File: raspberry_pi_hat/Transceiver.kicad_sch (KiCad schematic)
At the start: 6 parts, among them IC2 LM3940IT, J2 USB_C_Receptacle_PowerOnly_6P, J3 GPIO, U1 NRF24L01P

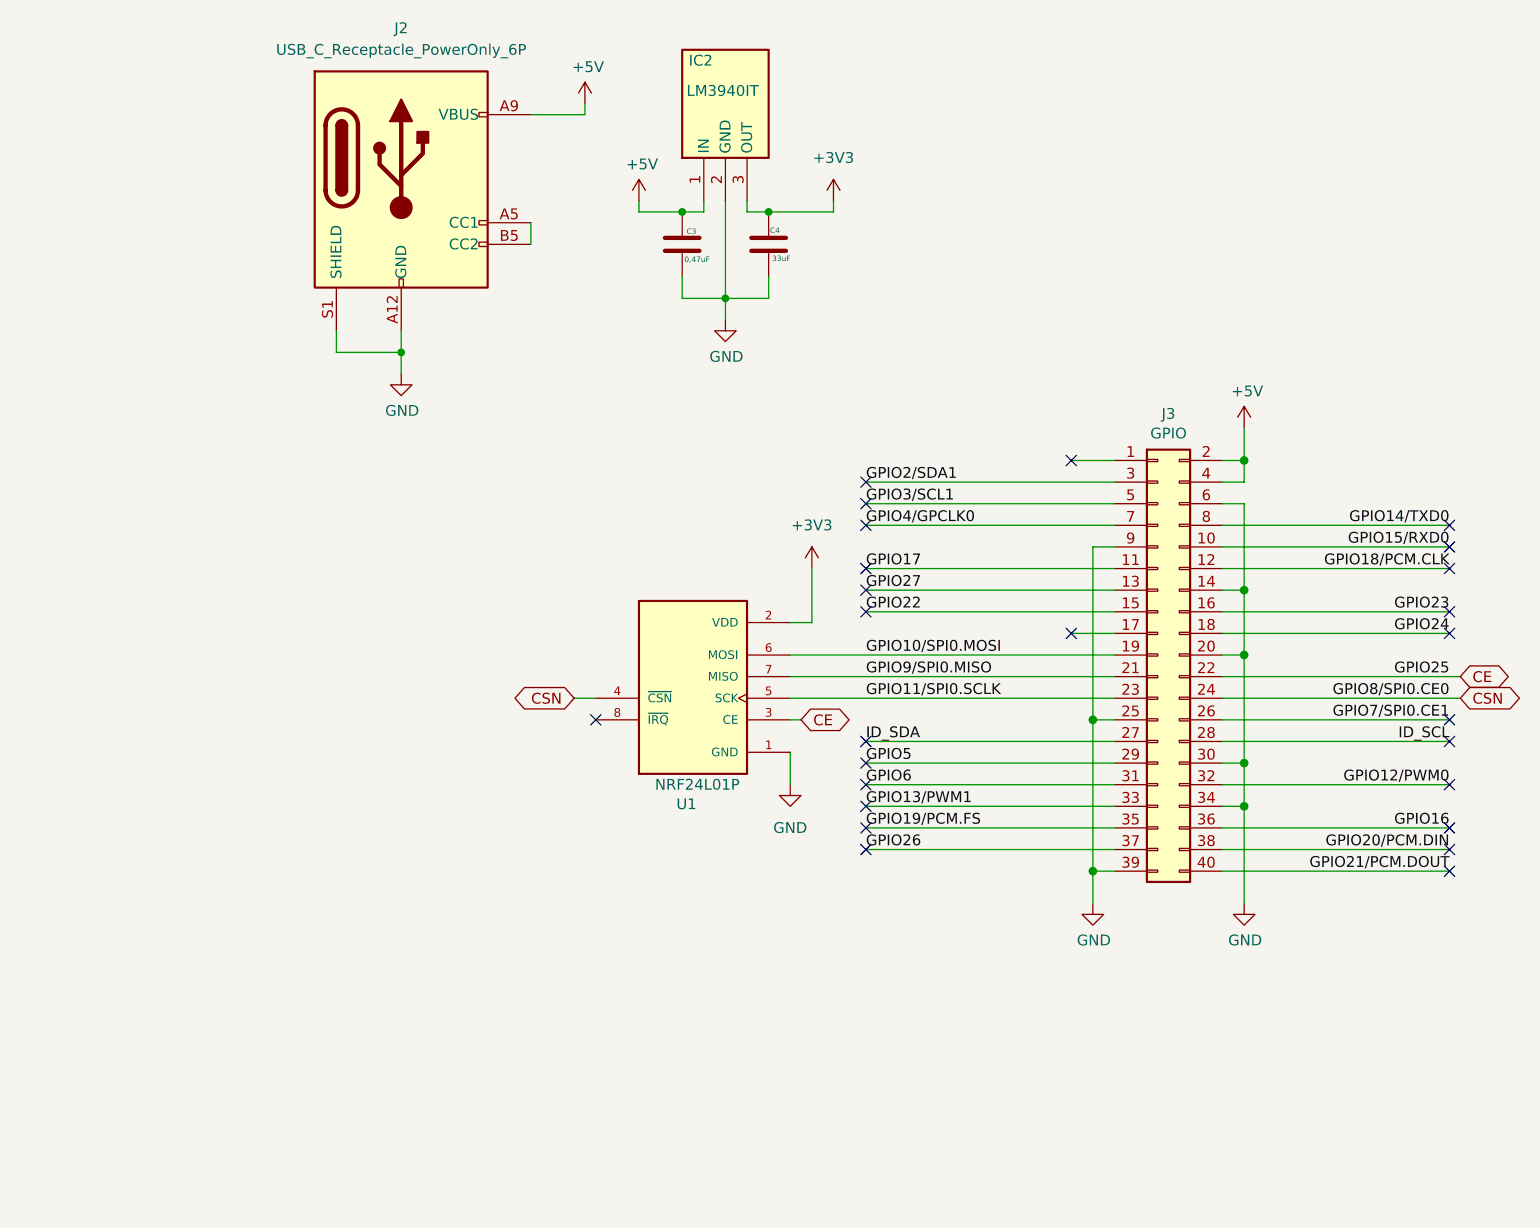
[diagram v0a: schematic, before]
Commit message: Solved split connection issues between boards
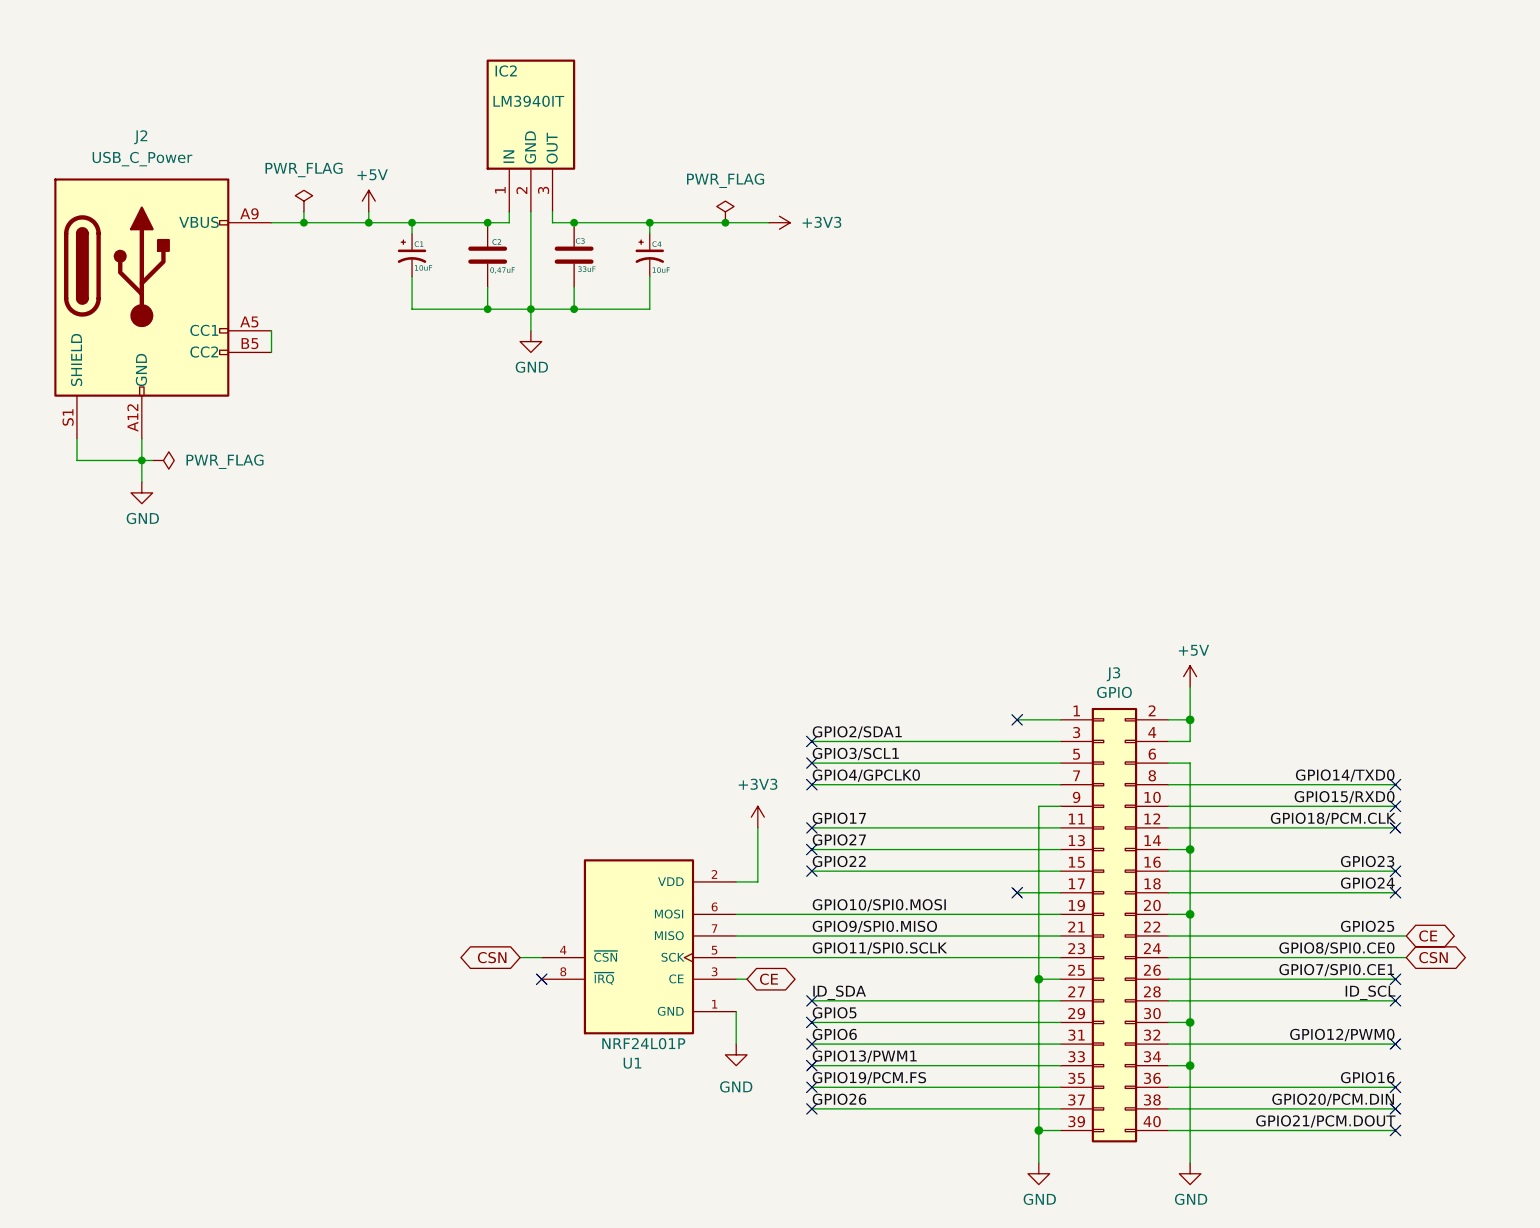
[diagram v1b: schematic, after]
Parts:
- added C1, C4: 10uF, Capacitor_THT:CP_Radial_D5.0mm_P2.50mm, symbol Device:C_Polarized_Small_US
- IC2: footprint Package_TO_SOT_THT:TO-262-3-1EP_Horizontal_TabDown -> Package_TO_SOT_THT:TO-220F-3_Horizontal_TabDown
- J2: value USB_C_Receptacle_PowerOnly_6P -> USB_C_Power
- renumbered C3 to C2, C4 to C3
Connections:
- net +3V3: now also C4.1
- net +5V: now also C1.1
- net GND: now also C1.2, C4.2
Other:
- moved on the sheet: C2, C3, IC2, J2, J3, U1

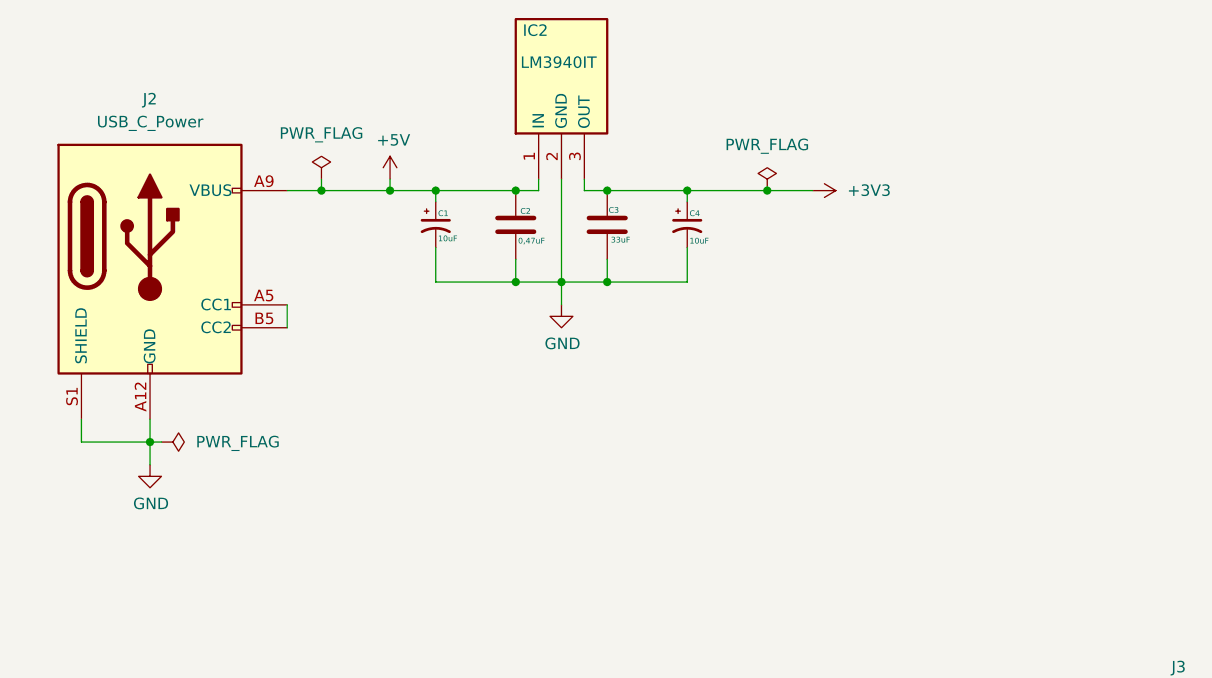
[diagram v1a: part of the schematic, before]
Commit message: Changed boards orientation and redistribution of components, still being 2 boards
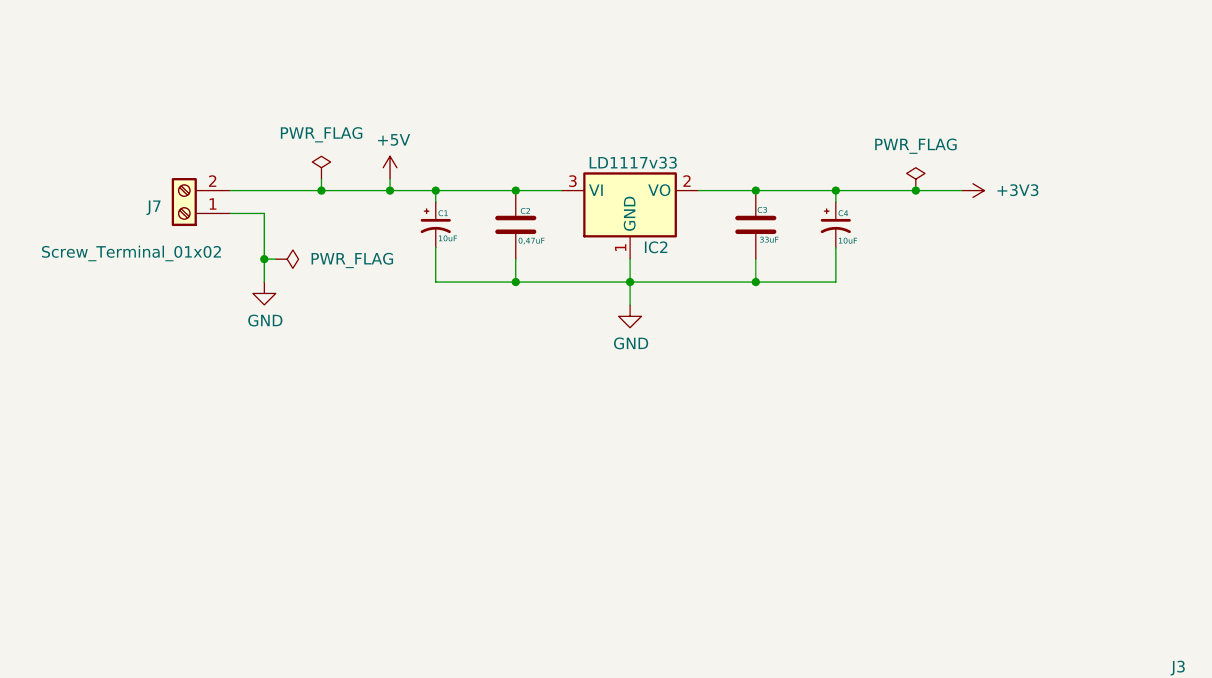
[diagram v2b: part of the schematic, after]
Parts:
- removed J2: USB_C_Power, Connector_USB:USB_C_Receptacle_GCT_USB4125-xx-x-0190_6P_TopMnt_Horizontal, symbol Connector:USB_C_Receptacle_PowerOnly_6P
- added J7: Screw_Terminal_01x02, TerminalBlock_MetzConnect:TerminalBlock_MetzConnect_Type101_RT01602HBWC_1x02_P5.08mm_Horizontal, symbol Connector:Screw_Terminal_01x02
- IC2: value LM3940IT -> LD1117v33; footprint Package_TO_SOT_THT:TO-220F-3_Horizontal_TabDown -> Package_TO_SOT_THT:TO-220-3_Vertical; symbol LM3940IT-3_3-NOPB:LM3940IT-3.3_NOPB -> Regulator_Linear:LD1117S33TR_SOT223
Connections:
- net +3V3: now also IC2.2 (VO); no longer IC2.3 (OUT)
- net +5V: now also IC2.3 (VI), J7.2 (Pin_2); no longer IC2.1 (IN)
- net GND: now also IC2.1 (GND), J7.1 (Pin_1); no longer IC2.2 (GND)
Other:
- moved on the sheet: C3, C4, IC2

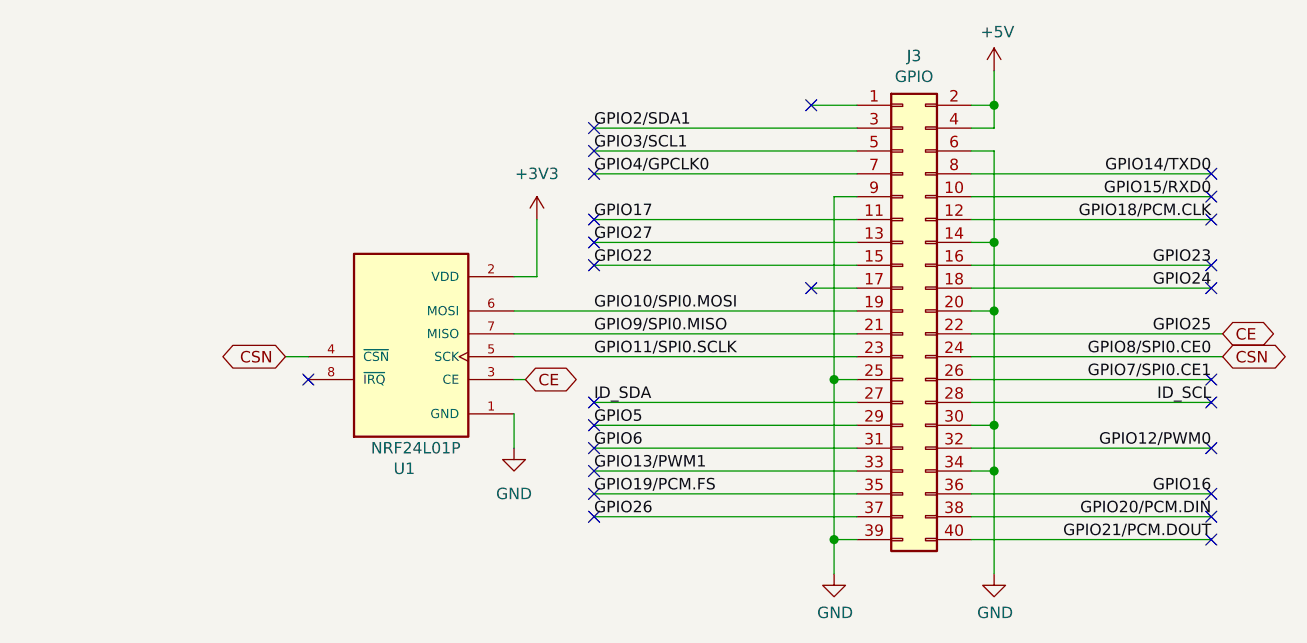
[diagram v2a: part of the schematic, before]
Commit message: Completed redistribution of boards
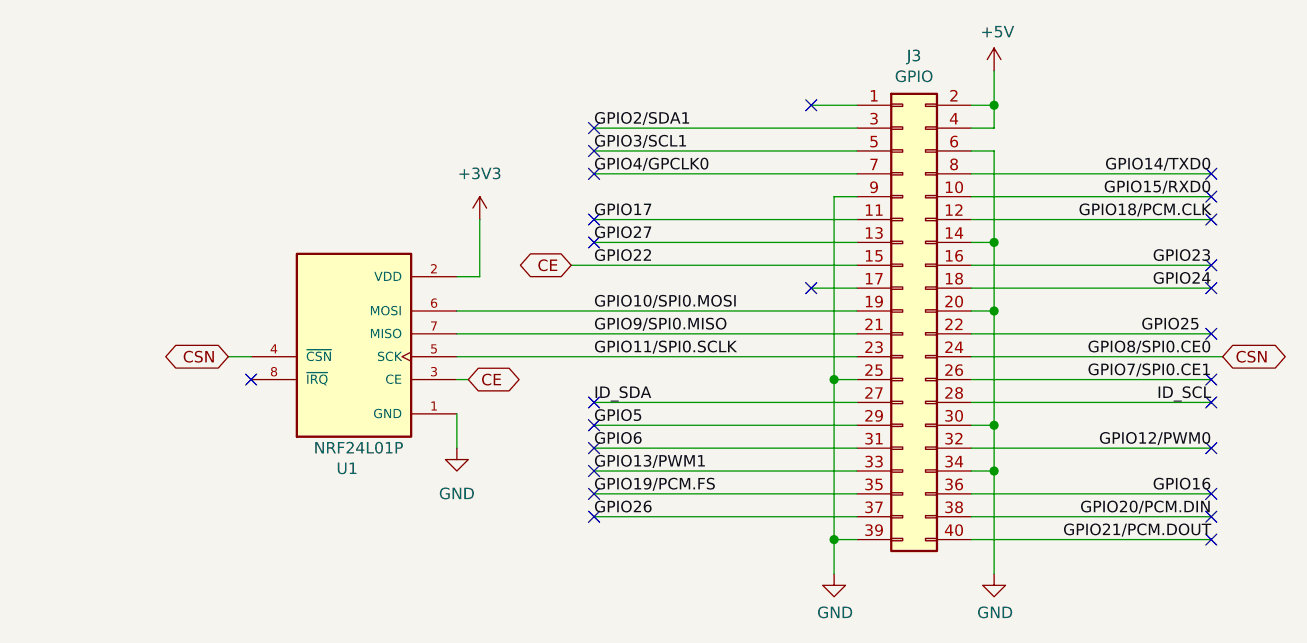
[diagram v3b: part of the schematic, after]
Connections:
- net GPIO22 is gone; now on net CE: J3.15 (Pin_15)
- net CE: no longer J3.22 (Pin_22)
- new net GPIO25: J3.22 (Pin_22)
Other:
- moved on the sheet: U1
